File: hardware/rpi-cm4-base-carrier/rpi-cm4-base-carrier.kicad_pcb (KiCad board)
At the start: 4 copper layers, 168.9 x 141.1 mm, 80 parts, among them IC1 KTD2052BEVAA-TR, J1 690-019-298-412, J10 Conn_02x05_Odd_Even, J11 XM7B-0442, J2 DNP, J3 USB4105-GF-A, J5 THD-02-R, J6 JT4-1202HL, J7 Micro_SD_Card_Det, J9 690-008-221-904, U1 RT9742SNGV, U4 RT9742GGJ5, U5 FSUSB42MUX, U6 USB2514B-I/M2, U8 AP22653W6, U9 74LVC1G07SE-7, Y1 CX3225CA24000D0HSSCC

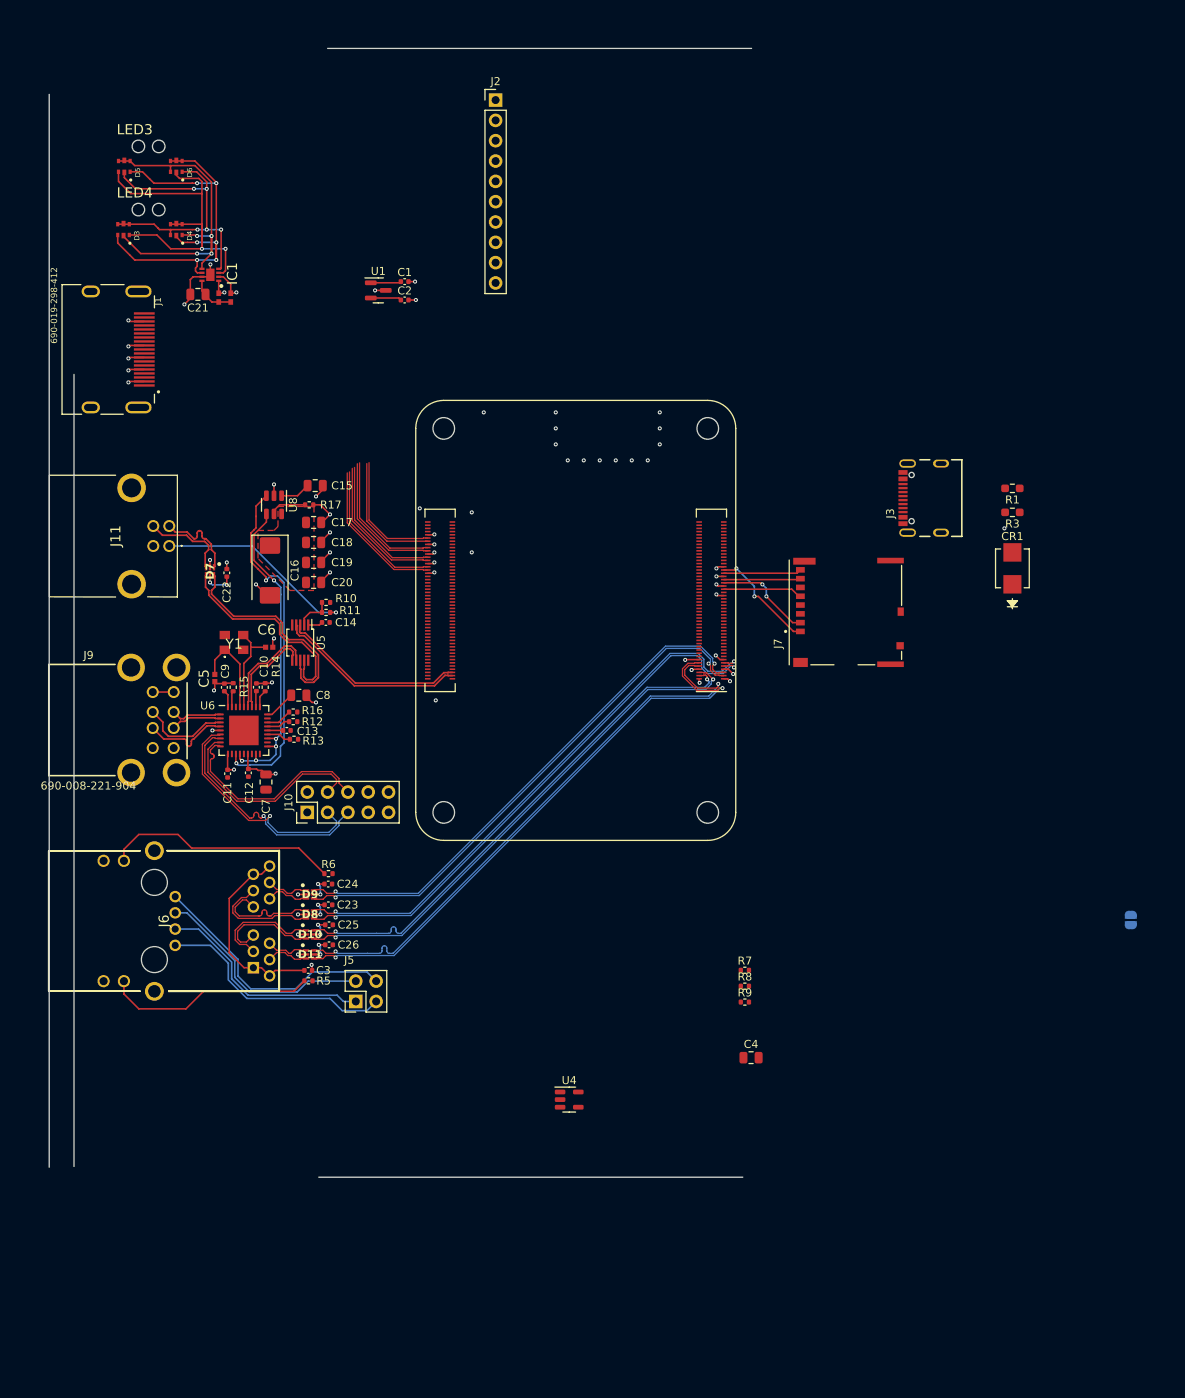
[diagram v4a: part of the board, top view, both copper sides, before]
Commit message: schematic entry for samtec board edge connector complete, started breakout of GPIO lines for connection to board edge connector
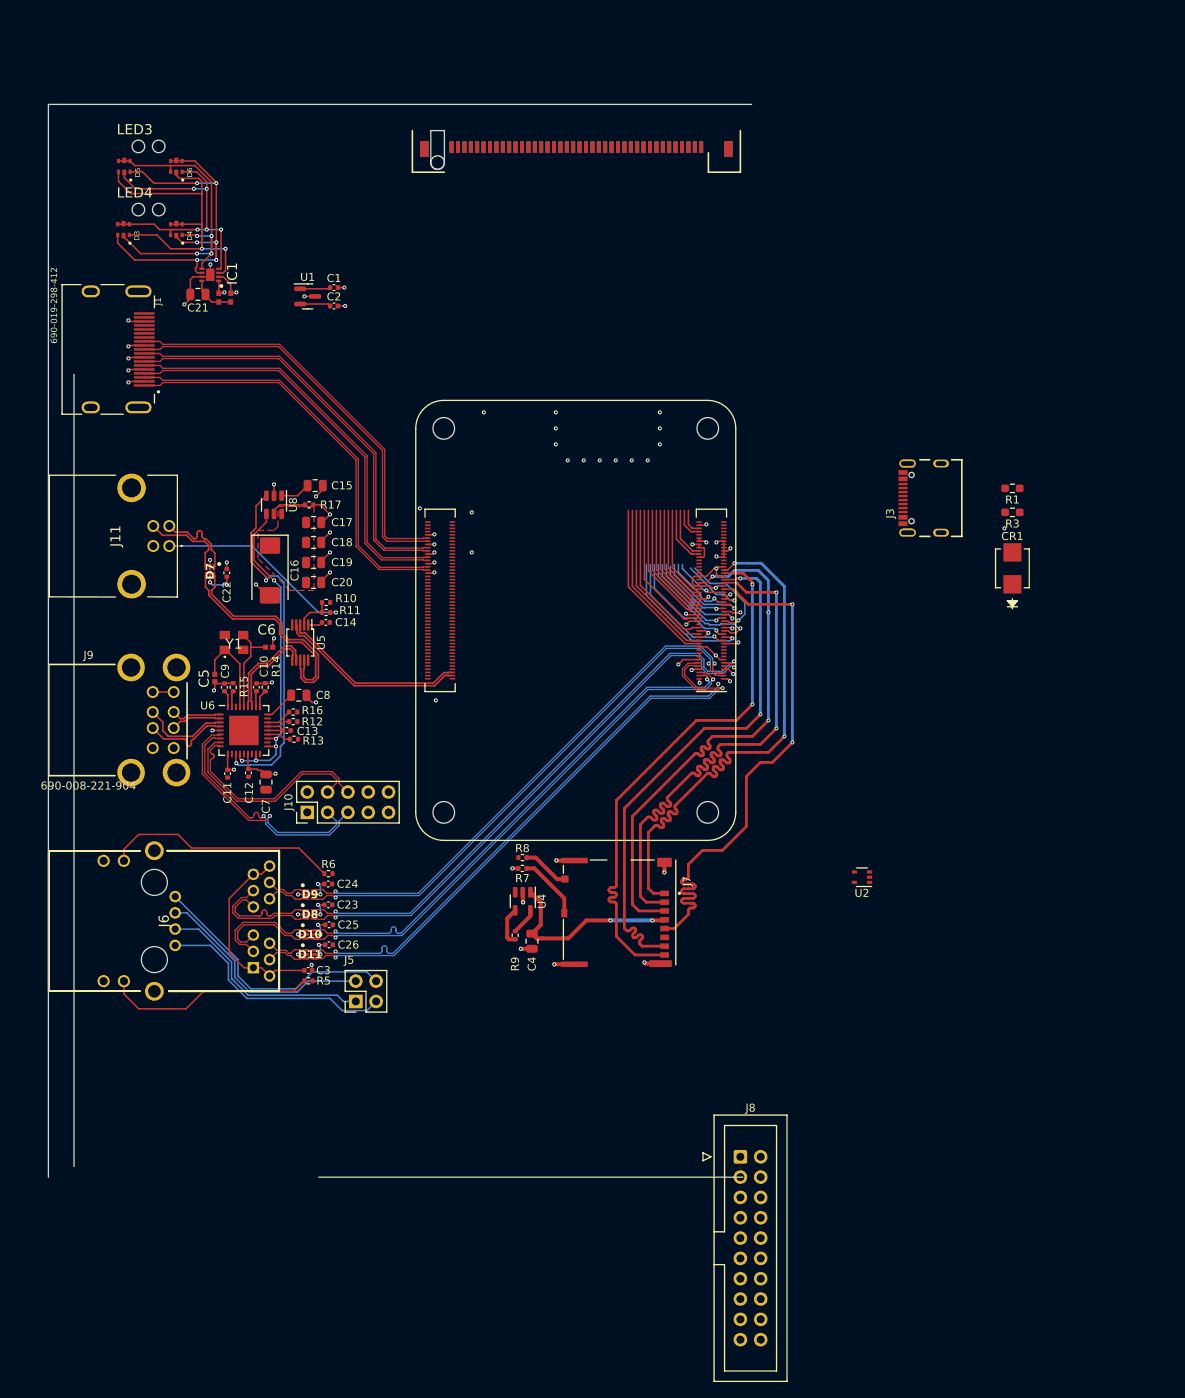
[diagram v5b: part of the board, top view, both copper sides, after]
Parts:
- removed JP1: SolderJumper_2_Open, Jumper:SolderJumper-2_P1.3mm_Open_RoundedPad1.0x1.5mm
- added J8: Conn_02x10_Odd_Even, Connector_IDC:IDC-Header_2x10_P2.54mm_Vertical, F.Cu at (166.5, 171.6)
- added U2: 74LVC1G07SE-7, Package_TO_SOT_SMD:SOT-353_SC-70-5, F.Cu at (181.7, 136.6)
- J2: value DNP -> ERM8-040-01-X-D-EM2-L-XX; footprint Connector_PinHeader_2.54mm:PinHeader_1x10_P2.54mm_Vertical -> ERM8-040-01-L-D-EM2-L-TR:SAMTEC_ERM8-040-01-X-D-EM2-L-XX; moved to B.Cu
- moved J7 46.9 mm to (151.4, 141.0), turned to -90 degrees
- moved R8 32.1 mm to (139.3, 134.2)
- moved C4 31.0 mm to (140.4, 144.6), turned to -90 degrees
- moved R7 30.6 mm to (139.2, 135.5)
- moved R9 29.9 mm to (138.3, 143.9), turned to -90 degrees
- moved U4 25.5 mm to (139.3, 139.6), turned to -90 degrees
- moved J2 10.8 mm to (146.0, 43.3), turned to 180 degrees
- moved C1 8.87 mm to (115.7, 62.9)
- moved C2 8.87 mm to (115.7, 65.2)
- moved U1 8.87 mm to (112.4, 64.0)
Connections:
- J2 pad 10: /CM4 GPIO/nRPIBOOT -> GND
- Module1 pad 145: unconnected-(Module1B-HDMI1_SDA-Pad145) -> /Board_Edge_Connector/HDMI1_SDA
- Module1 pad 147: unconnected-(Module1B-HDMI1_SCL-Pad147) -> /Board_Edge_Connector/HDMI1_SCL
- Module1 pad 16: unconnected-(Module1A-Ethernet_SYNC_IN(1.8v)-Pad16) -> /Board_Edge_Connector/SYNC_IN
- Module1 pad 18: unconnected-(Module1A-Ethernet_SYNC_OUT(1.8v)-Pad18) -> /Board_Edge_Connector/SYNC_OUT
- Module1 pad 20: /CM4 GPIO/EEPROM_nWP -> /Board_Edge_Connector/EEPROM_nWP
- Module1 pad 24: unconnected-(Module1A-GPIO26-Pad24) -> /Board_Edge_Connector/GPIO26
- Module1 pad 25: unconnected-(Module1A-GPIO21-Pad25) -> /Board_Edge_Connector/GPIO21
- Module1 pad 26: unconnected-(Module1A-GPIO19-Pad26) -> /Board_Edge_Connector/GPIO19
- Module1 pad 27: unconnected-(Module1A-GPIO20-Pad27) -> /Board_Edge_Connector/GPIO20
- Module1 pad 28: unconnected-(Module1A-GPIO13-Pad28) -> GND
- Module1 pad 29: unconnected-(Module1A-GPIO16-Pad29) -> /Board_Edge_Connector/GPIO16
- Module1 pad 30: unconnected-(Module1A-GPIO6-Pad30) -> /Board_Edge_Connector/GPIO6
- Module1 pad 31: unconnected-(Module1A-GPIO12-Pad31) -> /Board_Edge_Connector/GPIO12
- Module1 pad 34: unconnected-(Module1A-GPIO5-Pad34) -> /Board_Edge_Connector/GPIO5
- Module1 pad 37: /CM4 GPIO/GPIO7 -> /Board_Edge_Connector/GPIO7
- Module1 pad 38: /CM4 GPIO/GPIO11 -> GND
- Module1 pad 39: /CM4 GPIO/GPIO8 -> /Board_Edge_Connector/GPIO8
- Module1 pad 40: /CM4 GPIO/GPIO9 -> /Board_Edge_Connector/GPIO9
- Module1 pad 41: unconnected-(Module1A-GPIO25-Pad41) -> /Board_Edge_Connector/GPIO25
- Module1 pad 44: /CM4 GPIO/GPIO10 -> /Board_Edge_Connector/GPIO10
- Module1 pad 45: unconnected-(Module1A-GPIO24-Pad45) -> /Board_Edge_Connector/GPIO24
- Module1 pad 46: unconnected-(Module1A-GPIO22-Pad46) -> /Board_Edge_Connector/GPIO22
- Module1 pad 47: unconnected-(Module1A-GPIO23-Pad47) -> /Board_Edge_Connector/GPIO23
- Module1 pad 48: unconnected-(Module1A-GPIO27-Pad48) -> /Board_Edge_Connector/GPIO27
- Module1 pad 49: unconnected-(Module1A-GPIO18-Pad49) -> /Board_Edge_Connector/GPIO18
- Module1 pad 50: unconnected-(Module1A-GPIO17-Pad50) -> /Board_Edge_Connector/GPIO17
- Module1 pad 51: /CM4 GPIO/GPIO15 -> /Board_Edge_Connector/GPIO15
- Module1 pad 54: unconnected-(Module1A-GPIO4-Pad54) -> /Board_Edge_Connector/GPIO4
- Module1 pad 55: /CM4 GPIO/GPIO14 -> /Board_Edge_Connector/GPIO14
- Module1 pad 56: /CM4 GPIO/GPIO3 -> /Board_Edge_Connector/GPIO3
- Module1 pad 58: /CM4 GPIO/GPIO2 -> /Board_Edge_Connector/GPIO2
- Module1 pad 76: unconnected-(Module1A-Reserved-Pad76) -> /SDCard/Reserved
- Module1 pad 88: +3V3 -> +1V8
- Module1 pad 90: +3V3 -> +1V8
- Module1 pad 92: unconnected-(Module1A-RUN_PG-Pad92) -> /Board_Edge_Connector/RUN_PG
- Module1 pad 93: /CM4 GPIO/nRPIBOOT -> /Board_Edge_Connector/nRPIBOOT
- Module1 pad 94: unconnected-(Module1A-AnalogIP0-Pad94) -> /Board_Edge_Connector/AIN0
- Module1 pad 96: unconnected-(Module1A-AnalogIP1-Pad96) -> /Board_Edge_Connector/AIN1
- Module1 pad 99: unconnected-(Module1A-Global_EN-Pad99) -> /Board_Edge_Connector/GLOBAL_EN
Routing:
- net /CM4 GPIO/SD_CMD: track 0.00 -> 66.8 mm, vias 0 -> 3
- net /CM4 GPIO/SD_DAT1: track 9.75 -> 67.9 mm, vias 0 -> 2
- net /CM4 GPIO/SD_CLK: track 9.94 -> 67.9 mm, vias 0 -> 2
- net /CM4 GPIO/SD_DAT0: track 9.63 -> 66.8 mm, vias 0 -> 2
- net /CM4 GPIO/SD_DAT3: track 12.2 -> 68.2 mm
- net /CM4 GPIO/SD_DAT2: track 13.7 -> 66.6 mm
- net /CM4 High Speed/HDMI0_CK_N: track 15.5 -> 52.0 mm
- net /CM4 High Speed/HDMI0_CK_P: track 15.8 -> 52.0 mm
- net GND: track 91.7 -> 127.8 mm, vias 61 -> 74
- net /CM4 High Speed/HDMI0_D0_N: track 17.0 -> 51.9 mm
- net /CM4 High Speed/HDMI0_D0_P: track 17.3 -> 51.9 mm
- net /CM4 High Speed/HDMI0_D1_N: track 17.7 -> 51.7 mm
- net /CM4 High Speed/HDMI0_D1_P: track 18.0 -> 51.7 mm
- net /CM4 High Speed/HDMI0_D2_N: track 18.4 -> 51.6 mm
- net /CM4 High Speed/HDMI0_D2_P: track 18.7 -> 51.6 mm
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- added copper zone on In2.Cu, net +3V3
- added copper zone on In1.Cu, net GND
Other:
- board size 168.9 x 141.1 mm -> 169 x 134.1 mm

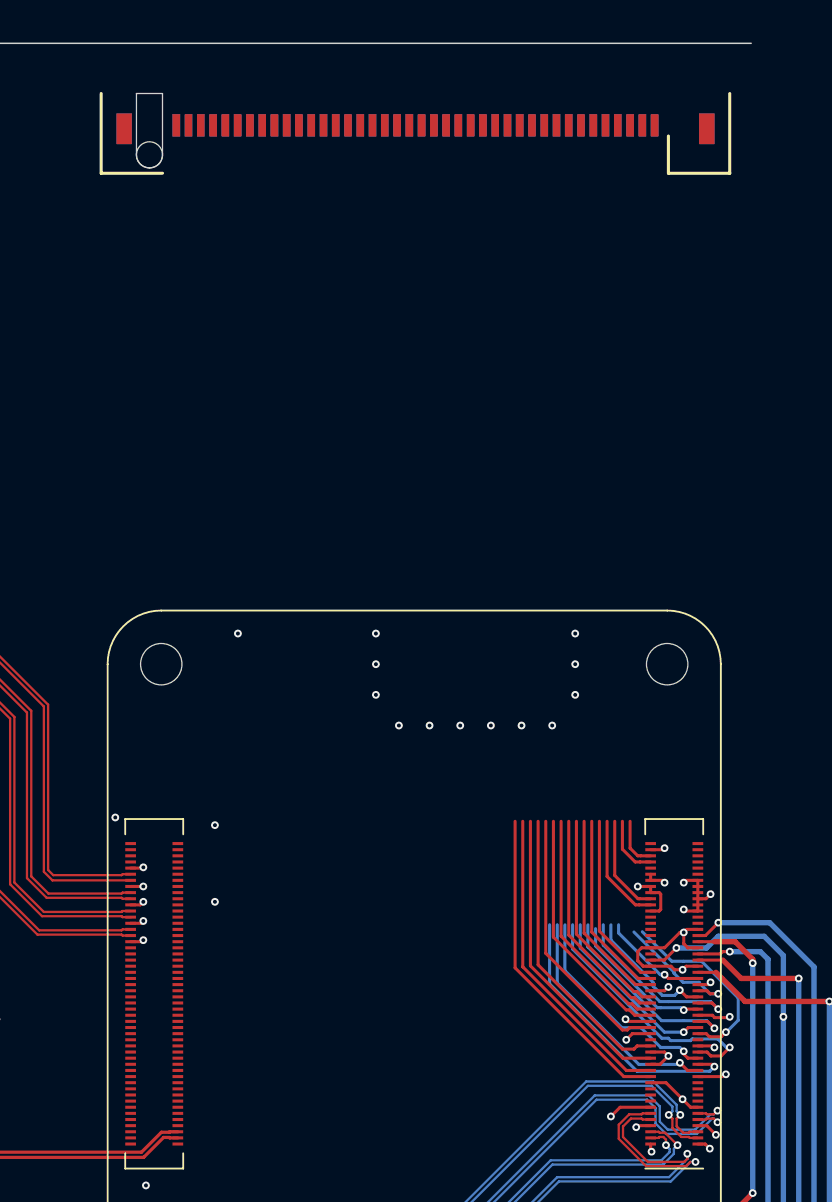
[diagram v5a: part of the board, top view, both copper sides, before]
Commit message: board edge connector mostly connected
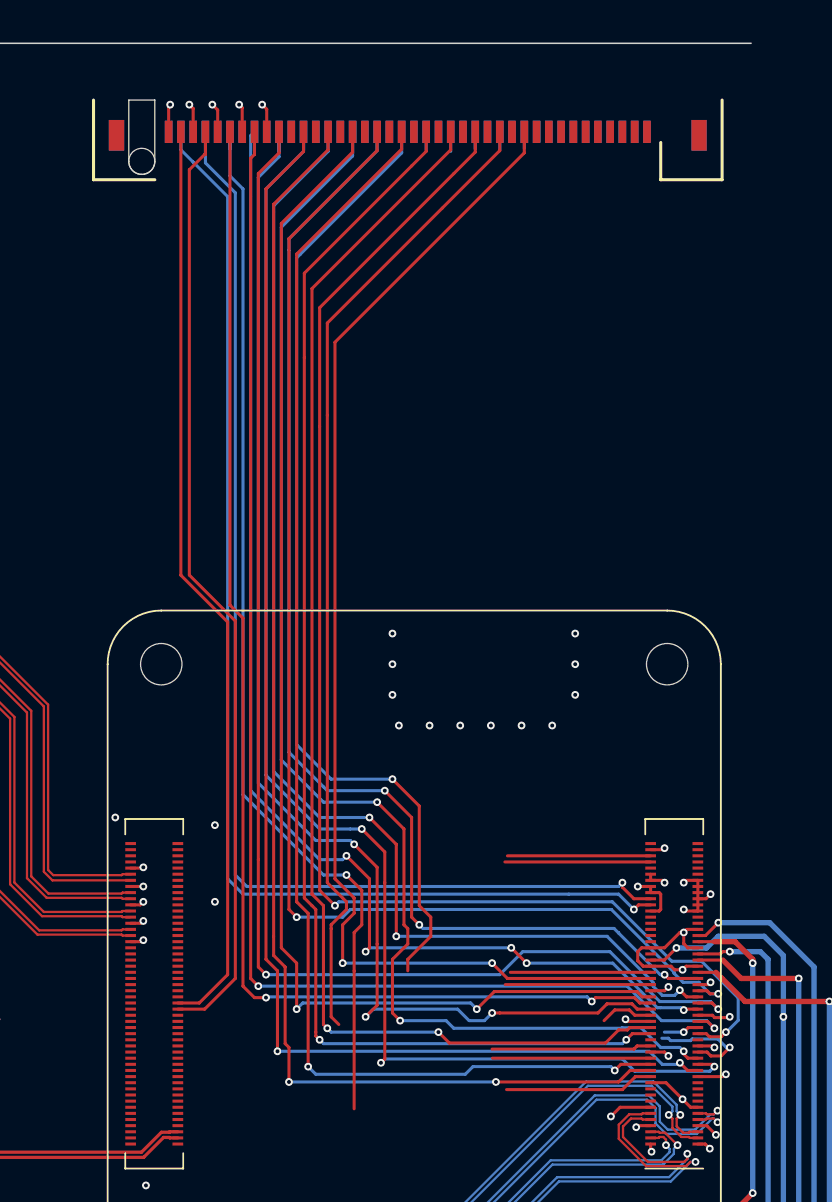
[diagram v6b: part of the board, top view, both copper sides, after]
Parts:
- moved J2 0.66 mm to (145.5, 43.7)
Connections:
- J2 pad 03: /Board_Edge_Connector/GPIO2 -> /CM4 GPIO/SCL0
- J2 pad 04: /Board_Edge_Connector/GPIO3 -> /Board_Edge_Connector/HDMI1_SCL
- J2 pad 07: /Board_Edge_Connector/GPIO4 -> /CM4 GPIO/SDA0
- J2 pad 08: /Board_Edge_Connector/GPIO5 -> /Board_Edge_Connector/HDMI1_SDA
- J2 pad 11: /Board_Edge_Connector/GPIO6 -> /Board_Edge_Connector/GPIO26
- J2 pad 12: /Board_Edge_Connector/GPIO7 -> /Board_Edge_Connector/GPIO27
- J2 pad 15: /Board_Edge_Connector/GPIO8 -> /Board_Edge_Connector/GPIO24
- J2 pad 16: /Board_Edge_Connector/GPIO9 -> /Board_Edge_Connector/GPIO25
- J2 pad 19: /Board_Edge_Connector/GPIO10 -> /Board_Edge_Connector/GPIO22
- J2 pad 20: unconnected-(J2-Pad20) -> /Board_Edge_Connector/GPIO23
- J2 pad 23: /Board_Edge_Connector/GPIO12 -> /Board_Edge_Connector/GPIO20
- J2 pad 24: unconnected-(J2-Pad24) -> /Board_Edge_Connector/GPIO21
- J2 pad 27: /Board_Edge_Connector/GPIO14 -> /Board_Edge_Connector/GPIO18
- J2 pad 28: /Board_Edge_Connector/GPIO15 -> /Board_Edge_Connector/GPIO19
- J2 pad 35: /Board_Edge_Connector/GPIO18 -> /Board_Edge_Connector/GPIO14
- J2 pad 36: /Board_Edge_Connector/GPIO19 -> /Board_Edge_Connector/GPIO15
- J2 pad 39: /Board_Edge_Connector/GPIO20 -> /Board_Edge_Connector/GPIO12
- J2 pad 40: /Board_Edge_Connector/GPIO21 -> /Board_Edge_Connector/GPIO13
- J2 pad 43: /Board_Edge_Connector/GPIO22 -> /Board_Edge_Connector/GPIO10
- J2 pad 44: /Board_Edge_Connector/GPIO23 -> /Board_Edge_Connector/GPIO11
- J2 pad 47: /Board_Edge_Connector/GPIO24 -> /Board_Edge_Connector/GPIO8
- J2 pad 48: /Board_Edge_Connector/GPIO25 -> /Board_Edge_Connector/GPIO9
- J2 pad 51: /Board_Edge_Connector/GPIO26 -> /Board_Edge_Connector/GPIO6
- J2 pad 52: /Board_Edge_Connector/GPIO27 -> /Board_Edge_Connector/GPIO7
- J2 pad 55: /CM4 GPIO/SDA0 -> /Board_Edge_Connector/GPIO4
- J2 pad 56: /Board_Edge_Connector/HDMI1_SDA -> /Board_Edge_Connector/GPIO5
- J2 pad 59: /CM4 GPIO/SCL0 -> /Board_Edge_Connector/GPIO2
- J2 pad 60: /Board_Edge_Connector/HDMI1_SCL -> /Board_Edge_Connector/GPIO3
- J2 pad 63: +3V3 -> +20V
- J2 pad 64: +5V -> +20V
- J2 pad 67: +3V3 -> +20V
- J2 pad 68: +5V -> +20V
- J2 pad 75: +20V -> +3V3
- J2 pad 76: +20V -> +5V
- J2 pad 79: +20V -> +3V3
- J2 pad 80: +20V -> +5V
- J8 pad 6: GND -> /Board_Edge_Connector/GPIO11
- Module1 pad 28: GND -> /Board_Edge_Connector/GPIO13
- Module1 pad 38: GND -> /Board_Edge_Connector/GPIO11
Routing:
- net /Board_Edge_Connector/GPIO13: track 0.00 -> 87.1 mm, vias 0 -> 2
- net /Board_Edge_Connector/GPIO11: track 0.00 -> 84.9 mm, vias 0 -> 2
- net /Board_Edge_Connector/GPIO23: track 12.0 -> 88.9 mm, vias 1 -> 2
- net /Board_Edge_Connector/GPIO15: track 8.64 -> 85.3 mm, vias 1 -> 2
- net /Board_Edge_Connector/GPIO7: track 12.7 -> 88.7 mm, vias 1 -> 2
- net /Board_Edge_Connector/GPIO25: track 13.2 -> 88.2 mm, vias 1 -> 2
- net /Board_Edge_Connector/GPIO21: track 15.4 -> 89.3 mm, vias 1 -> 2
- net /Board_Edge_Connector/GPIO24: track 9.56 -> 83.0 mm, vias 1 -> 5
- net /Board_Edge_Connector/GPIO20: track 18.2 -> 91.3 mm, vias 1 -> 3
- net /Board_Edge_Connector/GPIO14: track 6.93 -> 79.5 mm, vias 1 -> 3
- net /Board_Edge_Connector/GPIO16: track 14.1 -> 86.6 mm, vias 1 -> 3
- net /Board_Edge_Connector/GPIO18: track 8.64 -> 80.9 mm, vias 1 -> 3
- net /CM4 GPIO/SCL0: track 9.51 -> 80.8 mm, vias 1 -> 2
- net /CM4 GPIO/SDA0: track 10.3 -> 81.2 mm, vias 1 -> 2
- net /Board_Edge_Connector/GPIO17: track 13.9 -> 83.6 mm, vias 0 -> 2
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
